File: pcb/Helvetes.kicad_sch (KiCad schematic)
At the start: 17 parts

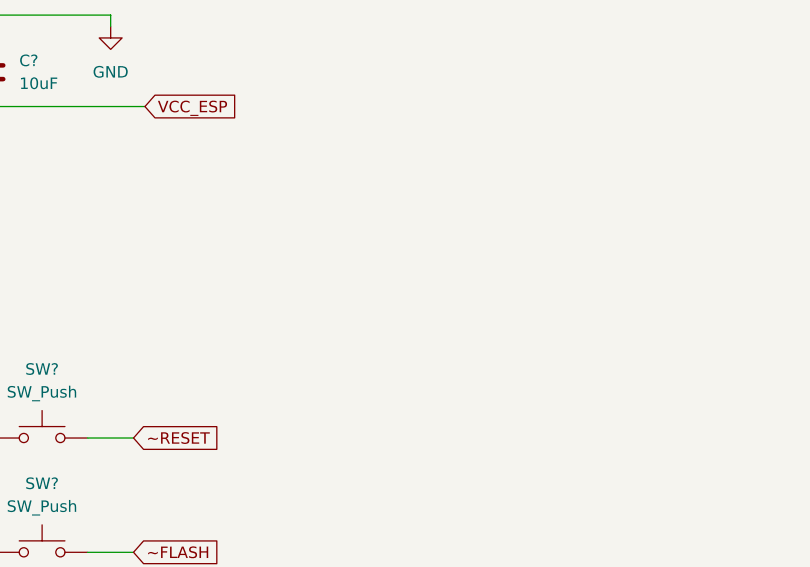
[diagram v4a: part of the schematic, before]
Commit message: :construction: Add a connector for flashing the MCU firmware
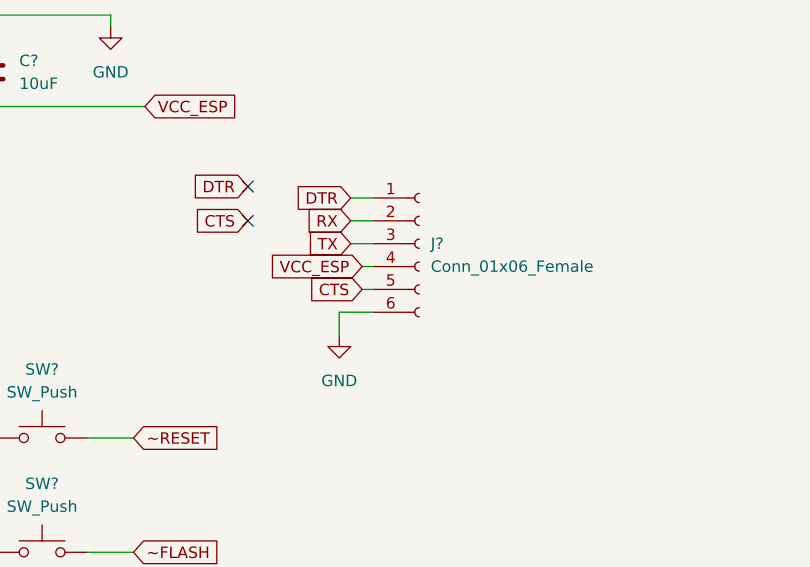
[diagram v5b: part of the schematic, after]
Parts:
- added J?: Conn_01x06_Female, symbol Connector:Conn_01x06_Female
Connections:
- net GND: now also J?.6 (Pin_6)
- net RX: now also J?.2 (Pin_2)
- net TX: now also J?.3 (Pin_3)
- net VCC_ESP: now also J?.4 (Pin_4)
- new net CTS: J?.5 (Pin_5)
- new net DTR: J?.1 (Pin_1)
- no-connect marks 12 -> 14
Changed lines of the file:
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@@
   (no_connect (at 71.12 82.55))
   (no_connect (at 71.12 80.01))
+  (no_connect (at 121.92 39.37))
+  (no_connect (at 121.92 35.56))
   (no_connect (at 24.13 182.88))
   (no_connect (at 24.13 177.8))
@@
     (stroke (width 0) (type default) (color 0 0 0 0))
   )
+  (wire (pts (xy 133.35 36.83) (xy 135.89 36.83))
+    (stroke (width 0) (type default) (color 0 0 0 0))
+  )
   (wire (pts (xy 259.08 34.29) (xy 259.08 40.64))
     (stroke (width 0) (type default) (color 0 0 0 0))
@@
     (stroke (width 0) (type default) (color 0 0 0 0))
   )
+  (wire (pts (xy 132.08 49.53) (xy 132.08 52.07))
+    (stroke (width 0) (type default) (color 0 0 0 0))
+  )
   (wire (pts (xy 106.68 16.51) (xy 106.68 17.78))
     (stroke (width 0) (type default) (color 0 0 0 0))
@@
     (stroke (width 0) (type default) (color 0 0 0 0))
   )
+  (wire (pts (xy 133.35 41.91) (xy 135.89 41.91))
+    (stroke (width 0) (type default) (color 0 0 0 0))
+  )
   (wire (pts (xy 63.5 177.8) (xy 63.5 180.34))
     (stroke (width 0) (type default) (color 0 0 0 0))
@@
     (stroke (width 0) (type default) (color 0 0 0 0))
   )
+  (wire (pts (xy 134.62 44.45) (xy 135.89 44.45))
+    (stroke (width 0) (type default) (color 0 0 0 0))
+  )
   (wire (pts (xy 63.5 152.4) (xy 67.31 152.4))
     (stroke (width 0) (type default) (color 0 0 0 0))
@@
     (stroke (width 0) (type default) (color 0 0 0 0))
   )
+  (wire (pts (xy 134.62 46.99) (xy 135.89 46.99))
+    (stroke (width 0) (type default) (color 0 0 0 0))
+  )
   (wire (pts (xy 15.24 165.1) (xy 15.24 170.18))
     (stroke (width 0) (type default) (color 0 0 0 0))
@@
     (stroke (width 0) (type default) (color 0 0 0 0))
   )
+  (wire (pts (xy 135.89 49.53) (xy 132.08 49.53))
+    (stroke (width 0) (type default) (color 0 0 0 0))
+  )
   (wire (pts (xy 257.81 151.13) (xy 260.35 151.13))
     (stroke (width 0) (type default) (color 0 0 0 0))
@@
   )
   (wire (pts (xy 80.01 19.05) (xy 80.01 16.51))
+    (stroke (width 0) (type default) (color 0 0 0 0))
+  )
+  (wire (pts (xy 133.35 39.37) (xy 135.89 39.37))
     (stroke (width 0) (type default) (color 0 0 0 0))
   )
@@
     )
   )
+  (global_label "DTR" (shape input) (at 121.92 35.56 180) (fields_autoplaced)
+    (effects (font (size 1.27 1.27)) (justify right))
+    (property "Intersheet References" "${INTERSHEET_REFS}" (id 0) (at 115.9993 35.4806 0)
+      (effects (font (size 1.27 1.27)) (justify right) hide)
+    )
+  )
   (global_label "~RESET" (shape input) (at 109.22 63.5 0) (fields_autoplaced)
     (effects (font (size 1.27 1.27)) (justify left))
@@
     )
   )
+  (global_label "TX" (shape input) (at 133.35 41.91 180) (fields_autoplaced)
+    (effects (font (size 1.27 1.27)) (justify right))
+    (property "Intersheet References" "${INTERSHEET_REFS}" (id 0) (at 128.7598 41.8306 0)
+      (effects (font (size 1.27 1.27)) (justify right) hide)
+    )
+  )
   (global_label "TX" (shape input) (at 36.83 39.37 180) (fields_autoplaced)
     (effects (font (size 1.27 1.27)) (justify right))
@@
     )
   )
+  (global_label "VCC_ESP" (shape input) (at 134.62 44.45 180) (fields_autoplaced)
+    (effects (font (size 1.27 1.27)) (justify right))
+    (property "Intersheet References" "${INTERSHEET_REFS}" (id 0) (at 123.9821 44.3706 0)
+      (effects (font (size 1.27 1.27)) (justify right) hide)
+    )
+  )
+  (global_label "DTR" (shape input) (at 133.35 36.83 180) (fields_autoplaced)
+    (effects (font (size 1.27 1.27)) (justify right))
+    (property "Intersheet References" "${INTERSHEET_REFS}" (id 0) (at 127.4293 36.7506 0)
+      (effects (font (size 1.27 1.27)) (justify right) hide)
+    )
+  )
   (global_label "RX" (shape input) (at 31.75 36.83 180) (fields_autoplaced)
     (effects (font (size 1.27 1.27)) (justify right))
@@
     )
   )
+  (global_label "CTS" (shape input) (at 134.62 46.99 180) (fields_autoplaced)
+    (effects (font (size 1.27 1.27)) (justify right))
+    (property "Intersheet References" "${INTERSHEET_REFS}" (id 0) (at 128.7598 46.9106 0)
+      (effects (font (size 1.27 1.27)) (justify right) hide)
+    )
+  )
   (global_label "~FLASH" (shape input) (at 109.22 76.2 0) (fields_autoplaced)
     (effects (font (size 1.27 1.27)) (justify left))
@@
     )
   )
+  (global_label "CTS" (shape input) (at 121.92 39.37 180) (fields_autoplaced)
+    (effects (font (size 1.27 1.27)) (justify right))
+    (property "Intersheet References" "${INTERSHEET_REFS}" (id 0) (at 116.0598 39.2906 0)
+      (effects (font (size 1.27 1.27)) (justify right) hide)
+    )
+  )
   (global_label "TempData" (shape output) (at 271.78 142.24 0) (fields_autoplaced)
     (effects (font (size 1.27 1.27)) (justify left))
@@
     )
   )
+  (global_label "RX" (shape input) (at 133.35 39.37 180) (fields_autoplaced)
+    (effects (font (size 1.27 1.27)) (justify right))
+    (property "Intersheet References" "${INTERSHEET_REFS}" (id 0) (at 128.4574 39.2906 0)
+      (effects (font (size 1.27 1.27)) (justify right) hide)
+    )
+  )
   (symbol (lib_id "Device:C") (at 80.01 22.86 0) (unit 1)
     (in_bom yes) (on_board yes) (fields_autoplaced)
@@
     )
     (property "Datasheet" "" (id 3) (at 271.78 46.99 0)
+      (effects (font (size 1.27 1.27)) hide)
+    )
+    (pin "1")
+  )
+  (symbol (lib_id "power:GND") (at 132.08 52.07 0) (unit 1)
+    (in_bom yes) (on_board yes) (fields_autoplaced)
+    (property "Reference" "#PWR?" (id 0) (at 132.08 58.42 0)
+      (effects (font (size 1.27 1.27)) hide)
+    )
+    (property "Value" "GND" (id 1) (at 132.08 57.15 0))
+    (property "Footprint" "" (id 2) (at 132.08 52.07 0)
+      (effects (font (size 1.27 1.27)) hide)
+    )
+    (property "Datasheet" "" (id 3) (at 132.08 52.07 0)
       (effects (font (size 1.27 1.27)) hide)
     )
@@
     (pin "1")
   )
+  (symbol (lib_id "Connector:Conn_01x06_Female") (at 140.97 41.91 0) (unit 1)
+    (in_bom yes) (on_board yes) (fields_autoplaced)
+    (property "Reference" "J?" (id 0) (at 142.24 41.9099 0)
+      (effects (font (size 1.27 1.27)) (justify left))
+    )
+    (property "Value" "Conn_01x06_Female" (id 1) (at 142.24 44.4499 0)
+      (effects (font (size 1.27 1.27)) (justify left))
+    )
+    (property "Footprint" "" (id 2) (at 140.97 41.91 0)
+      (effects (font (size 1.27 1.27)) hide)
+    )
+    (property "Datasheet" "~" (id 3) (at 140.97 41.91 0)
+      (effects (font (size 1.27 1.27)) hide)
+    )
+    (pin "1")
+    (pin "2")
+    (pin "3")
+    (pin "4")
+    (pin "5")
+    (pin "6")
+  )
   (symbol (lib_id "Switch:SW_Push") (at 99.06 76.2 0) (unit 1)
     (in_bom yes) (on_board yes) (fields_autoplaced)
@@
       (reference "#PWR?") (unit 1) (value "GND") (footprint "")
     )
+    (path "/420271c2-554c-4e33-812e-84a2e99e030e"
+      (reference "#PWR?") (unit 1) (value "GND") (footprint "")
+    )
     (path "/599d37bf-e5d7-4e62-88ce-3397cea01f7d"
       (reference "#PWR?") (unit 1) (value "GND") (footprint "")
@@
       (reference "J?") (unit 1) (value "105450-0101") (footprint "MOLEX_105450-0101")
     )
+    (path "/806b945e-fc59-4641-ae29-5257d31d3d70"
+      (reference "J?") (unit 1) (value "Conn_01x06_Female") (footprint "")
+    )
     (path "/45d32487-e0d2-44ba-81a3-4a24d21e283c"

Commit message: :construction: Clean up the schematic
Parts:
- removed C? (x2): 22uF, symbol Device:C
- removed C? (x2): 100nF, symbol Device:C
- removed U?: AMS1117-5.0, Package_TO_SOT_SMD:SOT-223-3_TabPin2, symbol Regulator_Linear:AMS1117-5.0
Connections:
- net TempData: now also U?.10 (IO7)
- net VCC renamed +5V
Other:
- note added: "Buttons for resetting and flashing firmware"
- note added: "Controlling MCU"
- note added: "JTAG connector for flashing"
- note added: "Temperature Sensor (only rated to 150C, should be replaced)"
- note added: "USB-C Connector for Power (probably not used in final layout)"
- moved on the sheet: C?, J?, SW?, U?
